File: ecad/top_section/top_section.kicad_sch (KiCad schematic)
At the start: 11 parts, among them J1 JST PH, J2 JST PH, J3 JST SH, U11 MCP23017_ML

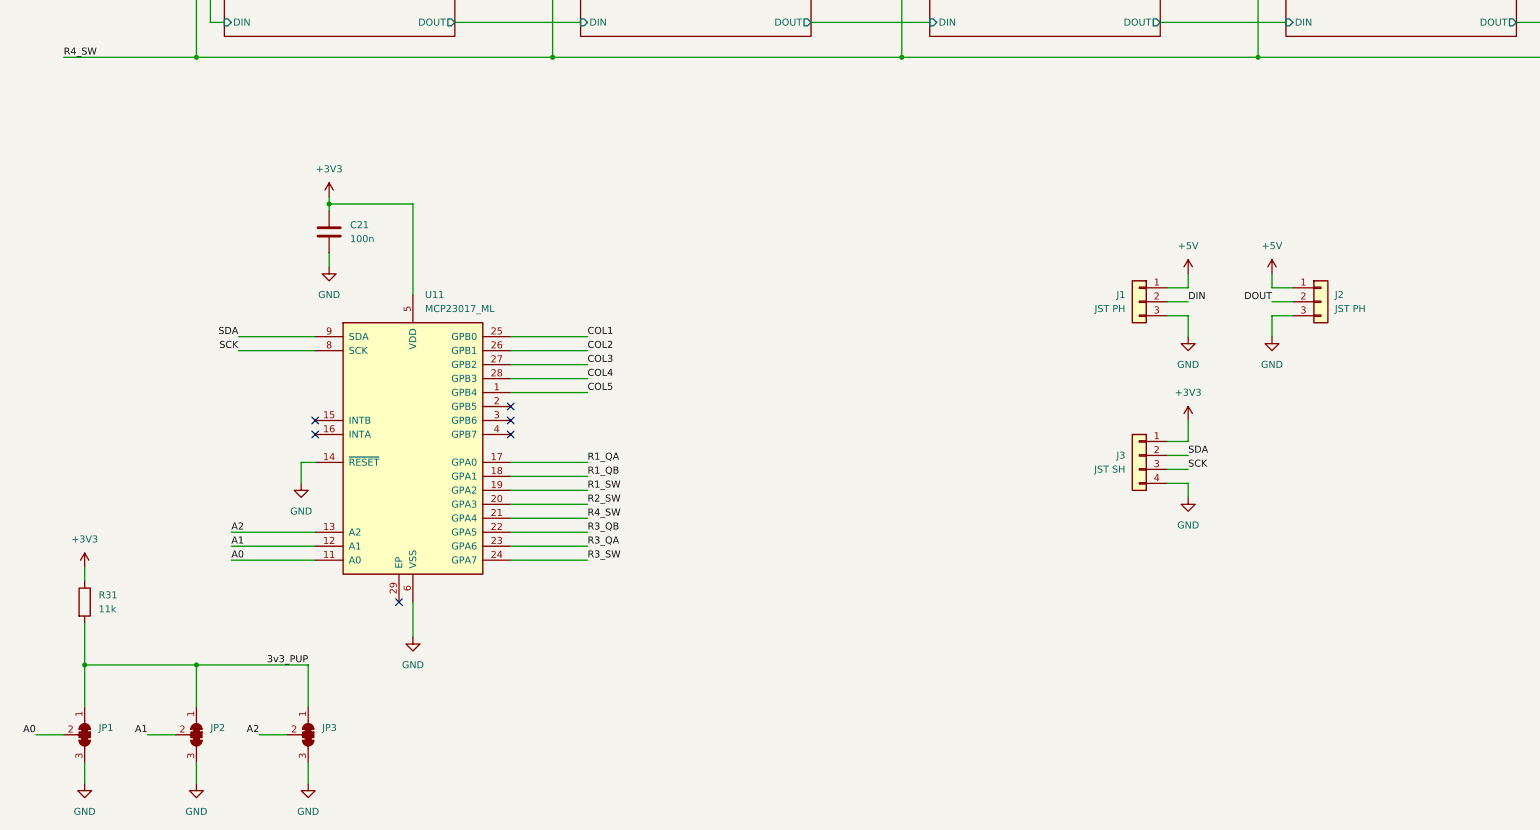
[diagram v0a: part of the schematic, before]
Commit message: Uses Attiny1617 MCU for ADC & Matrix RO
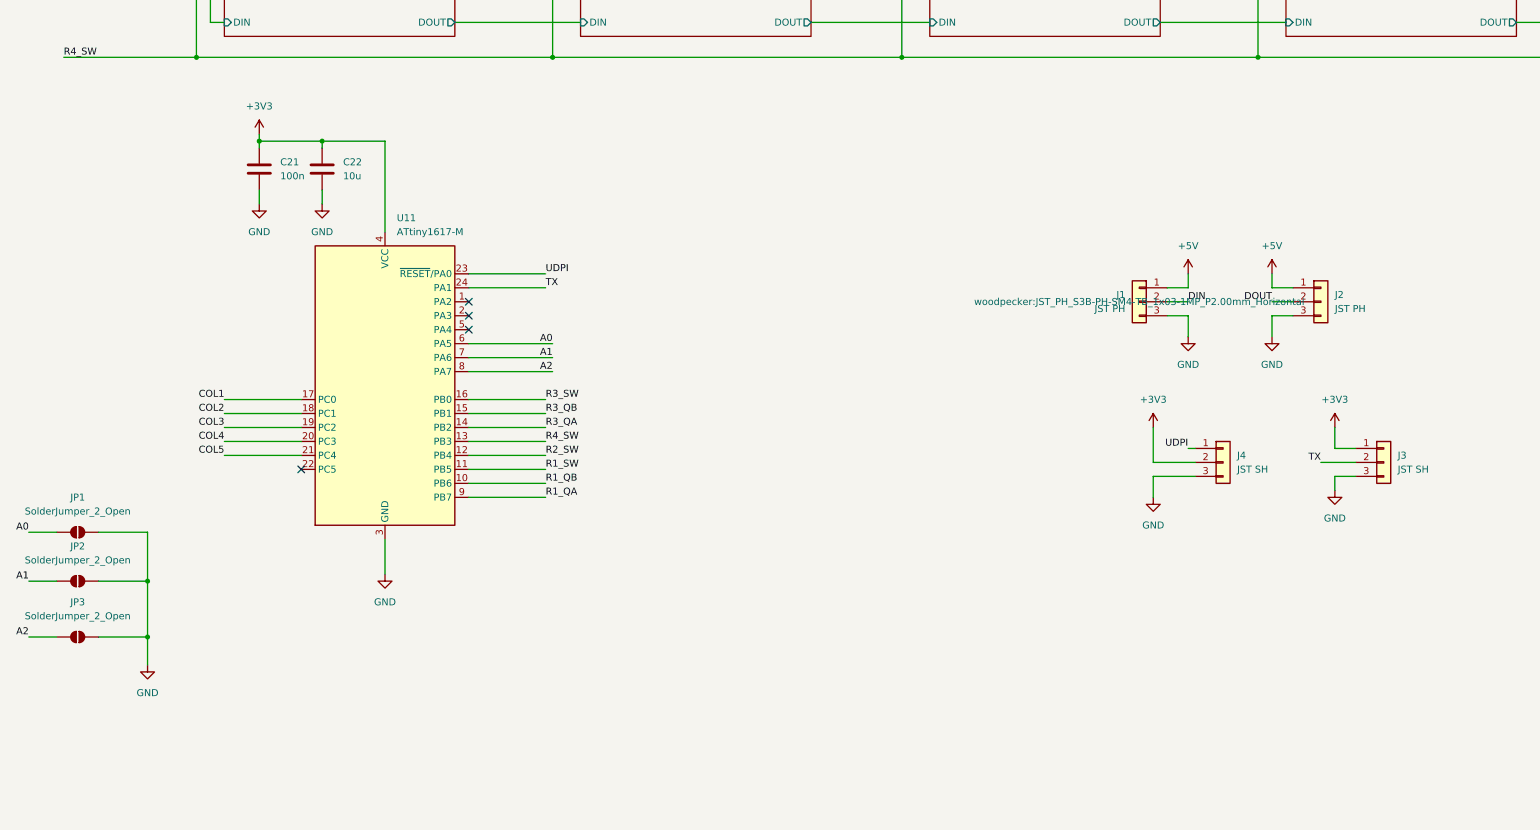
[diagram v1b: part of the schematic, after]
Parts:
- removed J3: JST SH, woodpecker:JST_SH_BM04B-SRSS-TB_1x04-1MP_P1.00mm_Vertical, symbol Connector_Generic:Conn_01x04
- removed JP1, JP2, JP3: ~, Jumper:SolderJumper-3_P2.0mm_Open_TrianglePad1.0x1.5mm, symbol Jumper:SolderJumper_3_Bridged123
- removed R31: 11k, Resistor_SMD:R_0603_1608Metric, symbol Device:R
- removed U11: MCP23017_ML, Package_DFN_QFN:QFN-28-1EP_6x6mm_P0.65mm_EP4.25x4.25mm, symbol Interface_Expansion:MCP23017_ML
- added C22: 10u, Capacitor_SMD:C_0603_1608Metric, symbol Device:C
- added J3, J4: JST SH, woodpecker:JST_SH_BM03B-SRSS-TB_1x03-1MP_P1.00mm_Vertical, symbol Connector_Generic:Conn_01x03
- added JP1, JP2, JP3: SolderJumper_2_Open, Jumper:SolderJumper-2_P1.3mm_Open_TrianglePad1.0x1.5mm, symbol Jumper:SolderJumper_2_Open
- added U11: ATtiny1617-M, Package_DFN_QFN:QFN-24-1EP_4x4mm_P0.5mm_EP2.6x2.6mm, symbol MCU_Microchip_ATtiny:ATtiny1617-M
- J1, J2: footprint woodpecker:JST_PH_B3B-PH-SM4-TB_1x03-1MP_P2.00mm_Vertical -> woodpecker:JST_PH_S3B-PH-SM4-TB_1x03-1MP_P2.00mm_Horizontal
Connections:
- net +3V3: now also C22.1, J3.1 (Pin_1), J4.2 (Pin_2), U11.4 (VCC)
- net A0: now also JP1.1 (A), U11.6 (PA5)
- net A1: now also JP2.1 (A), U11.7 (PA6)
- net A2: now also JP3.1 (A), U11.8 (PA7)
- net COL1: now also U11.17 (PC0)
- net COL2: now also U11.18 (PC1)
- net COL3: now also U11.19 (PC2)
- net COL4: now also U11.20 (PC3)
- net COL5: now also U11.21 (PC4)
- net GND: now also C22.2, J3.3 (Pin_3), J4.3 (Pin_3), JP1.2 (B), JP2.2 (B), JP3.2 (B), U11.25 (GND), U11.3 (GND)
- net R1_QA: now also U11.9 (PB7)
- net R1_QB: now also U11.10 (PB6)
- net R1_SW: now also U11.11 (PB5)
- net R2_SW: now also U11.12 (PB4)
- net R3_QA: now also U11.14 (PB2)
- net R3_QB: now also U11.15 (PB1)
- net R3_SW: now also U11.16 (PB0)
- net R4_SW: now also U11.13 (PB3)
- new net TX: J3.2 (Pin_2), U11.24 (PA1)
- new net UDPI: J4.1 (Pin_1), U11.23 (~{RESET}/PA0)
- no-connect marks 6 -> 4
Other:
- moved on the sheet: C21

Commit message: [WIP] Control board
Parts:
- removed C22: 10u, Capacitor_SMD:C_0603_1608Metric, symbol Device:C
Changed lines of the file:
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@@
 	)
 	(junction
-		(at 77.47 151.13)
-		(diameter 0)
-		(color 0 0 0 0)
-	)
-	(junction
 		(at 182.88 115.57)
 		(diameter 0)
@@
 	(wire
 		(pts
-			(xy 66.04 151.13) (xy 77.47 151.13)
+			(xy 66.04 151.13) (xy 88.9 151.13)
 		)
 		(stroke
@@
 	(wire
 		(pts
-			(xy 77.47 152.4) (xy 77.47 151.13)
-		)
-		(stroke
-			(width 0)
-			(type default)
-		)
-	)
-	(wire
-		(pts
 			(xy 236.22 93.98) (xy 229.87 93.98)
 		)
@@
 	(wire
 		(pts
-			(xy 77.47 151.13) (xy 88.9 151.13)
-		)
-		(stroke
-			(width 0)
-			(type default)
-		)
-	)
-	(wire
-		(pts
 			(xy 45.72 241.3) (xy 45.72 246.38)
 		)
@@
 	(wire
 		(pts
-			(xy 77.47 160.02) (xy 77.47 162.56)
-		)
-		(stroke
-			(width 0)
-			(type default)
-		)
-	)
-	(wire
-		(pts
 			(xy 308.61 44.45) (xy 308.61 60.96)
 		)
@@
 	)
 	(symbol
-		(lib_id "power:GND")
-		(at 77.47 162.56 0)
-		(unit 1)
-		(exclude_from_sim no)
-		(in_bom yes)
-		(on_board yes)
-		(dnp no)
-		(fields_autoplaced yes)
-		(property "Reference" "#PWR02"
-			(at 77.47 168.91 0)
-			(effects
-				(font
-					(size 1.27 1.27)
-				)
-				(hide yes)
-			)
-		)
-		(property "Value" "GND"
-			(at 77.47 167.64 0)
-			(effects
-				(font
-					(size 1.27 1.27)
-				)
-			)
-		)
-		(property "Footprint" ""
-			(at 77.47 162.56 0)
-			(effects
-				(font
-					(size 1.27 1.27)
-				)
-				(hide yes)
-			)
-		)
-		(property "Datasheet" ""
-			(at 77.47 162.56 0)
-			(effects
-				(font
-					(size 1.27 1.27)
-				)
-				(hide yes)
-			)
-		)
-		(property "Description" "Power symbol creates a global label with name \"GND\" , ground"
-			(at 77.47 162.56 0)
-			(effects
-				(font
-					(size 1.27 1.27)
-				)
-				(hide yes)
-			)
-		)
-		(pin "1"
-		)
-		(instances
-			(project "top_section"
-				(path "/908c4fb0-9cf3-4739-9176-bc5c47ef8a7b"
-					(reference "#PWR02")
-					(unit 1)
-				)
-			)
-		)
-	)
-	(symbol
 		(lib_id "Connector_Generic:Conn_01x03")
 		(at 270.51 209.55 0)
@@
 					(unit 1)
 				)
-			)
-		)
-	)
-	(symbol
-		(lib_id "Device:C")
-		(at 77.47 156.21 0)
-		(unit 1)
-		(exclude_from_sim no)
-		(in_bom yes)
-		(on_board yes)
-		(dnp no)
-		(fields_autoplaced yes)
-		(property "Reference" "C22"
-			(at 81.28 154.9399 0)
-			(effects
-				(font
-					(size 1.27 1.27)
-				)
-				(justify left)
-			)
-		)
-		(property "Value" "10u"
-			(at 81.28 157.4799 0)
-			(effects
-				(font
-					(size 1.27 1.27)
-				)
-				(justify left)
-			)
-		)
-		(property "Footprint" "Capacitor_SMD:C_0603_1608Metric"
-			(at 78.4352 160.02 0)
-			(effects
-				(font
-					(size 1.27 1.27)
-				)
-				(hide yes)
-			)
-		)
-		(property "Datasheet" "~"
-			(at 77.47 156.21 0)
-			(effects
-				(font
-					(size 1.27 1.27)
-				)
-				(hide yes)
-			)
-		)
-		(property "Description" "Unpolarized capacitor"
-			(at 77.47 156.21 0)
-			(effects
-				(font
-					(size 1.27 1.27)
-				)
-				(hide yes)
-			)
-		)
-		(pin "2"
-		)
-		(pin "1"
-		)
-		(instances
-			(project "top_section"
-				(path "/908c4fb0-9cf3-4739-9176-bc5c47ef8a7b"
-					(reference "C22")
-					(unit 1)
-				)

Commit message: WIP LED
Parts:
- removed R29: 33, Resistor_SMD:R_0603_1608Metric, symbol Device:R
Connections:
- net KeyboardKey_COL10/DOUT renamed KeyboardKey_COL10/LEDR
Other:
- sheet KeyboardKey_COL1 ports: added LEDA, LEDB, LEDG, LEDR; removed DIN, DOUT
- sheet KeyboardKey_COL10 ports: added LEDA, LEDB, LEDG, LEDR; removed DIN, DOUT
- sheet KeyboardKey_COL2 ports: added LEDA, LEDB, LEDG, LEDR; removed DIN, DOUT
- sheet KeyboardKey_COL3 ports: added LEDA, LEDB, LEDG, LEDR; removed DIN, DOUT
- sheet KeyboardKey_COL4 ports: added LEDA, LEDB, LEDG, LEDR; removed DIN, DOUT
- sheet KeyboardKey_COL5 ports: added LEDA, LEDB, LEDG, LEDR; removed DIN, DOUT
- sheet KeyboardKey_COL6 ports: added LEDA, LEDB, LEDG, LEDR; removed DIN, DOUT
- sheet KeyboardKey_COL7 ports: added LEDA, LEDB, LEDG, LEDR; removed DIN, DOUT
- sheet KeyboardKey_COL8 ports: added LEDA, LEDB, LEDG, LEDR; removed DIN, DOUT
- sheet KeyboardKey_COL9 ports: added LEDA, LEDB, LEDG, LEDR; removed DIN, DOUT
- sheet RotaryEncoder_COL1 ports: added LEDA, LEDB, LEDG, LEDR; removed DIN, DOUT, SW
- sheet RotaryEncoder_COL10 ports: added LEDA, LEDB, LEDG, LEDR; removed DIN, DOUT, SW
- sheet RotaryEncoder_COL2 ports: added LEDA, LEDB, LEDG, LEDR; removed DIN, DOUT, SW
- sheet RotaryEncoder_COL3 ports: added LEDA, LEDB, LEDG, LEDR; removed DIN, DOUT, SW
- sheet RotaryEncoder_COL4 ports: added LEDA, LEDB, LEDG, LEDR; removed DIN, DOUT, SW
- sheet RotaryEncoder_COL5 ports: added LEDA, LEDB, LEDG, LEDR; removed DIN, DOUT, SW
- sheet RotaryEncoder_COL6 ports: added LEDA, LEDB, LEDG, LEDR; removed DIN, DOUT, SW
- sheet RotaryEncoder_COL7 ports: added LEDA, LEDB, LEDG, LEDR; removed DIN, DOUT, SW
- sheet RotaryEncoder_COL8 ports: added LEDA, LEDB, LEDG, LEDR; removed DIN, DOUT, SW
- sheet RotaryEncoder_COL9 ports: added LEDA, LEDB, LEDG, LEDR; removed DIN, DOUT, SW
- moved on the sheet: C21, R27, U11

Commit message: [WIP] Layouting a matric led driver
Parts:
- removed R27: 33, Resistor_SMD:R_0603_1608Metric, symbol Device:R
- added C2, C3: 1u, Capacitor_SMD:C_0603_1608Metric, symbol Device:C
- added U2: LP5864, woodpecker:Texas_LP586X_VQFN-32-1EP_4x4mm_P0.4mm_EP2.8x2.8mm_ThermalVias, symbol woodpecker:LP5864
- renumbered C21 to C1, J4 to J2, J2 to J3, J3 to J4, U11 to U1
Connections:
- net +3V3: now also C2.1, U2.1 (VCC)
- net +5V: now also C3.1, U2.15 (VLED)
- net GND: now also C2.2, C3.2, U2.33 (GND)
- net R1_LEDA: now also U2.11 (SW0)
- net R2_LEDA: now also U2.12 (SW1)
- new net C1_LEDB: U2.2 (CS0)
- new net C1_LEDG: U2.3 (CS1)
- new net C1_LEDR: U2.4 (CS2)
- new net C2_LEDB: U2.5 (CS3)
- new net C2_LEDG: U2.6 (CS4)
- new net C2_LEDR: U2.7 (CS5)
- new net C3_LEDB: U2.8 (CS6)
- new net C3_LEDG: U2.9 (CS7)
- new net C3_LEDR: U2.10 (CS8)
- new net C4_LEDB: U2.16 (CS9)
- new net C4_LEDG: U2.17 (CS10)
- new net C4_LEDR: U2.18 (CS11)
- new net C5_LEDB: U2.19 (CS12)
- new net C5_LEDG: U2.20 (CS13)
- new net C5_LEDR: U2.21 (CS14)
- new net R3_LEDA: U2.13 (SW2)
- new net R4_LEDA: U2.14 (SW3)
- no-connect marks 4 -> 7
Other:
- moved on the sheet: J1, J2, J3, J4

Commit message: [WIP] Layouting a matric led driver
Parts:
- added C4: 1n, Capacitor_SMD:C_0402_1005Metric, symbol Device:C
- added C5: 1u, Capacitor_SMD:C_0402_1005Metric, symbol Device:C
- C2, C3: footprint Capacitor_SMD:C_0603_1608Metric -> Capacitor_SMD:C_0402_1005Metric
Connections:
- net GND: now also U2.26 (IF), U2.27 (VSYNC), C4.2, C5.2
- net at U2.25 (VCAP): now also C5.1
- net at U2.32 (VIO_EN): now also C4.1

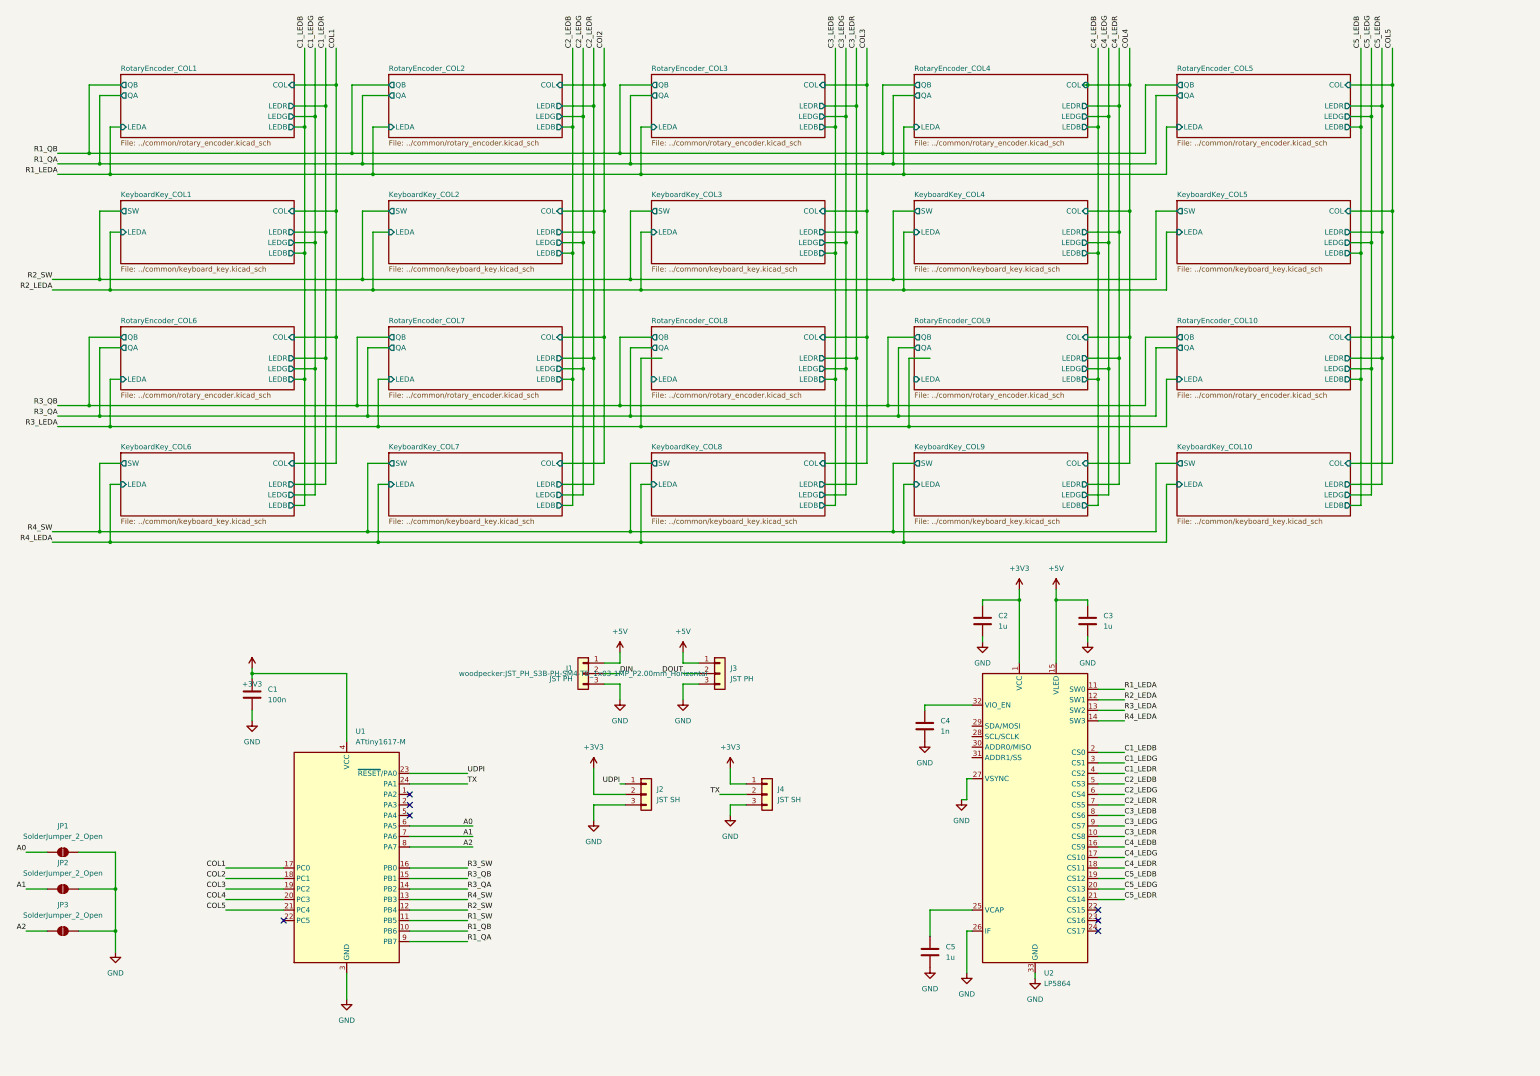
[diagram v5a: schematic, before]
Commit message: Uses a LP5864 LED Matrix Driver for Top Section
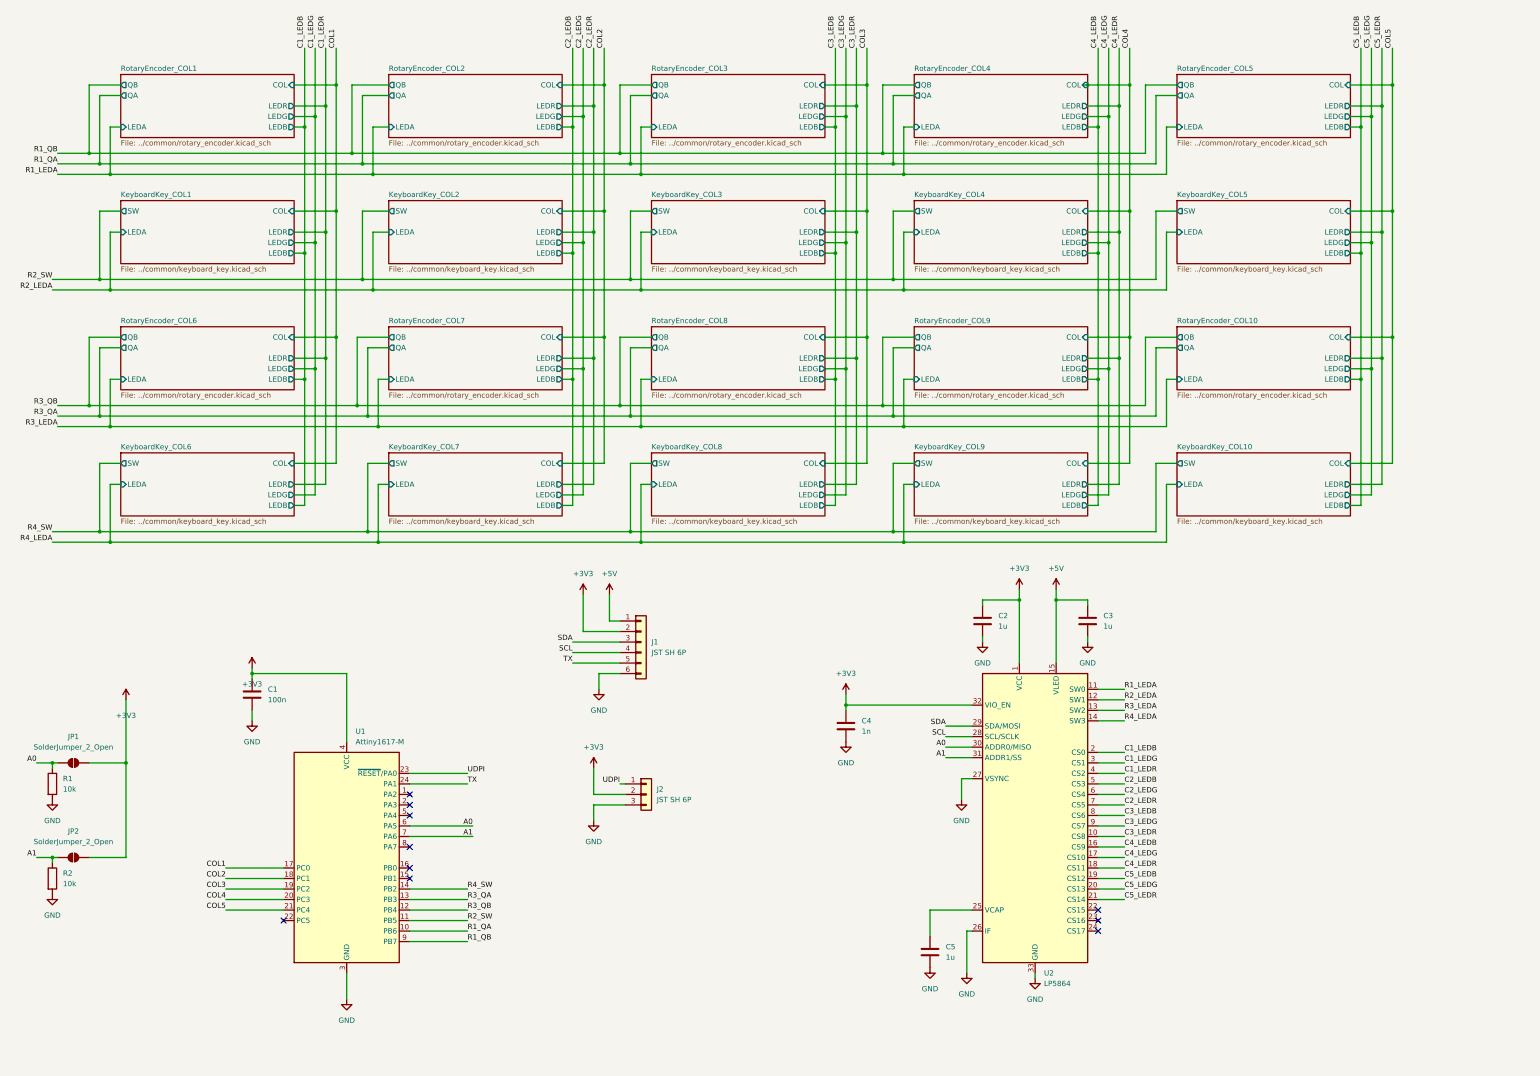
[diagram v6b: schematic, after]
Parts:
- removed J1, J3: JST PH, woodpecker:JST_PH_S3B-PH-SM4-TB_1x03-1MP_P2.00mm_Horizontal, symbol Connector_Generic:Conn_01x03
- removed J4: JST SH, woodpecker:JST_SH_BM03B-SRSS-TB_1x03-1MP_P1.00mm_Vertical, symbol Connector_Generic:Conn_01x03
- removed JP3: SolderJumper_2_Open, Jumper:SolderJumper-2_P1.3mm_Open_TrianglePad1.0x1.5mm, symbol Jumper:SolderJumper_2_Open
- added J1: JST SH 6P, Connector_JST:JST_SH_SM06B-SRSS-TB_1x06-1MP_P1.00mm_Horizontal, symbol Connector_Generic:Conn_01x06
- added R1, R2: 10k, Resistor_SMD:R_0603_1608Metric, symbol Device:R
- J2: value JST SH -> JST SH 6P; footprint woodpecker:JST_SH_BM03B-SRSS-TB_1x03-1MP_P1.00mm_Vertical -> woodpecker:JST_SH_SM03B-SRSS-TB_1x03-1MP_P1.00mm_Horizontal
- U1: value ATtiny1617-M -> Attiny1617-M; MPN (none) -> ATtiny1617-MNR
- U2: MPN (none) -> LP5864
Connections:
- net R1_SW is gone; now on net R2_SW: U1.11 (PB5)
- net +3V3: now also C4.1, JP1.2 (B), JP2.2 (B), U2.32 (VIO_EN), J1.2 (Pin_2)
- net +5V: now also J1.1 (Pin_1)
- net A0: now also U2.30 (ADDR0/MISO), R1.1
- net A1: now also U2.31 (ADDR1/SS), R2.1
- net GND: now also J1.6 (Pin_6), R1.2, R2.2; no longer JP1.2 (B), JP2.2 (B)
- net R1_QA: now also U1.10 (PB6); no longer U1.9 (PB7)
- net R1_QB: now also U1.9 (PB7); no longer U1.10 (PB6)
- net R2_SW: no longer U1.12 (PB4)
- net R3_QA: now also U1.13 (PB3); no longer U1.14 (PB2)
- net R3_QB: now also U1.12 (PB4); no longer U1.15 (PB1)
- net R4_SW: now also U1.14 (PB2); no longer U1.13 (PB3)
- net TX: now also J1.5 (Pin_5)
- net SCL: now reaches U2.28 (SCL/SCLK)
- net SCL: now also J1.4 (Pin_4)
- net SDA: now reaches U2.29 (SDA/MOSI)
- net SDA: now also J1.3 (Pin_3)
- net A2: no longer names the net of U1.8 (PA7)
- net R3_SW: no longer names the net of U1.16 (PB0)
- no-connect marks 7 -> 10
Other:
- moved on the sheet: C4, JP1, JP2
